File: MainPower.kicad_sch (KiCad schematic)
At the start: 70 parts, among them Q2 MBT2222ADW1T1, Q3 MBT2222ADW1T1, U10 ADM1176-1ARMZ-R7, U5 TPS259621DDA, U6 TPS54226PWPR, U7 ADM1176-1ARMZ-R7, U8 TPS259621DDA, U9 TPS54226PWPR

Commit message: v4.0 Updates
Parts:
- added R41: 100k, Resistor_SMD:R_0603_1608Metric, symbol Device:R_Small
- renumbered C31 to C29, C32 to C30, C33 to C31, C34 to C32, C35 to C33, C36 to C34, C37 to C35, C38 to C36, C39 to C37, C40 to C38, C41 to C39, C53 to C55, D8 to D10, D3 to D5, D4 to D6, D5 to D7, D6 to D8, D7 to D9, Q2 to Q3, Q3 to Q4, R20 to R22, R21 to R23, R22 to R24, R23 to R25, R24 to R26, R25 to R27, R26 to R28, R27 to R29, R29 to R30, R160 to R40, R41 to R42
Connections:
- net 3V3_P_EN: now also R41.1
- net GND: now also R41.2
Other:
- sheet I2C Protection5 renamed I2C Protection
- sheet I2C Protection7 renamed I2C Protection1
- moved on the sheet: R40

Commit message: DFM updates
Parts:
- C29, C42: DPN 587-3473-1-ND -> (none); DST Digi-Key -> (none); MFR Taiyo Yuden -> (none); MPN TMK107BJ105KAHT -> C2803395
- C30, C43: DPN 490-GCM32EC71E226KE36KCT-ND -> (none); DST Digi-Key -> (none); MFR Murata Electronics -> (none); MPN GCM32EC71E226KE36K -> C2214844
- C31, C44: DPN 399-14102-1-ND -> (none); DST Digi-Key -> (none); MFR KEMET -> (none); MPN C0603C103J3GECAUTO -> C161232
- C32, C33, C45, C46, C55: MPN (none) -> C386084
- C34, C39, C47, C52: MPN (none) -> C3877267
- C35, C48: MPN (none) -> C307348
- C36, C49: MPN (none) -> C2214844
- C37, C38, C50, C51: MPN (none) -> C2803395
- D5, D6, D7, D8: Author Antmicro -> (none); License Apache-2.0 -> (none); MPN LTST-C190GKT -> C2909774; Manufacturer Lite-On -> (none); Public False -> (none)
- L2, L3: Flight SPM5030T-3R3M-HZ -> (none); MPN (none) -> C518955; Manufacturer_Name TAI-TECH -> (none); Manufacturer_Part_Number HPC5040NF-3R3MTH -> (none); Proto HPC5040NF-3R3MTH -> (none)
- Q3: Flight MBT2222ADW1T1G -> (none); Manufacturer_Name ON Semiconductor -> (none); Manufacturer_Part_Number MBT2222ADW1T1G -> (none); Proto MBT2222ADW1T1G -> (none)
- R22: DPN RMCF0603FT10K0CT-ND -> (none); DST Digi-Key -> (none); MFR Stackpole Electronics Inc -> (none); MPN RMCF0603FT10K0 -> C844743
- R23: DPN RMCF0603FT10K0CT-ND -> (none); DST Digi-Key -> (none); MFR Stackpole Electronics Inc -> (none); MPN RMCF0603FT10K0 -> C844363
- R24: DPN RMCF0603FT604RCT-ND -> (none); DST Digi-Key -> (none); MFR Stackpole Electronics Inc -> (none); MPN RMCF0603FT604R -> C2091072
- R25, R35, R48: MPN (none) -> C843966
- R26, R36: MPN (none) -> C844759
- R27, R37, R49, R51: MPN (none) -> C237792
- R28, R38: value 0.01R -> 10m; MPN (none) -> C840621
- R29, R39: MPN (none) -> C2484712
- R30, R31, R43: MPN (none) -> C844915
- R32: DPN RMCF0603FT10K0CT-ND -> (none); DST Digi-Key -> (none); MFR Stackpole Electronics Inc -> (none); MPN RMCF0603FT10K0 -> C844796
- R33: DPN RMCF0603FT10K0CT-ND -> (none); DST Digi-Key -> (none); MFR Stackpole Electronics Inc -> (none); MPN RMCF0603FT10K0 -> C844734
- R40: DPN RMCF0603FT604RCT-ND -> (none); DST Digi-Key -> (none); MFR Stackpole Electronics Inc -> (none); MPN RMCF0603FT604R -> C2479067
- R41: DPN RMCF0603FT604RCT-ND -> (none); DST Digi-Key -> (none); MFR Stackpole Electronics Inc -> (none); MPN RMCF0603FT604R -> C237792
- R42: MPN (none) -> C402995
- R44, R45: Author Antmicro -> (none); License Apache-2.0 -> (none); MPN CR0402-FX-4701GLF -> C2479067; Manufacturer Bourns -> (none); Tolerance 1% -> (none); Val 4k7 -> (none)
- R46, R47: Author Antmicro -> (none); License Apache-2.0 -> (none); MPN CR0402-FX-4701GLF -> C844931; Manufacturer Bourns -> (none); Tolerance 1% -> (none); Val 4k7 -> (none)
- R50: MPN (none) -> C118142
- R52: MPN (none) -> C844923
- R53: MPN (none) -> C2479067
- U5, U8: DPN 296-TPS259620DDATCT-ND -> (none); DST Digi-Key -> (none); MFR Texas Instruments -> (none); MPN TPS259620DDAT -> C2155774

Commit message: Minor schematic fixes
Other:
- note added: "Vout = 0.765 * (1 + R25 / R26) Vout = 0.765 * (1 + 73.2k / 22.1k) Vout - 3.298V"
- note added: "Vout = 0.765 * (1 + R35 / R36) Vout = 0.765 * (1 + 73.2k / 22.1k) Vout - 3.298V"
- note removed: "Vout = 0.765 * (1 + R114 / R115) Vout = 0.765 * (1 + 73.2k / 22.1k) Vout - 3.298V"
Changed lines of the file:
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@@
 		)
 	)
-	(text "Vout = 0.765 * (1 + R114 / R115)\nVout = 0.765 * (1 + 73.2k / 22.1k)\nVout - 3.298V"
+	(text "Vout = 0.765 * (1 + R35 / R36)\nVout = 0.765 * (1 + 73.2k / 22.1k)\nVout - 3.298V"
 		(exclude_from_sim no)
 		(at 116.84 136.906 0)
@@
 		)
 	)
-	(text "Vout = 0.765 * (1 + R114 / R115)\nVout = 0.765 * (1 + 73.2k / 22.1k)\nVout - 3.298V"
+	(text "Vout = 0.765 * (1 + R25 / R26)\nVout = 0.765 * (1 + 73.2k / 22.1k)\nVout - 3.298V"
 		(exclude_from_sim no)
 		(at 112.268 68.326 0)

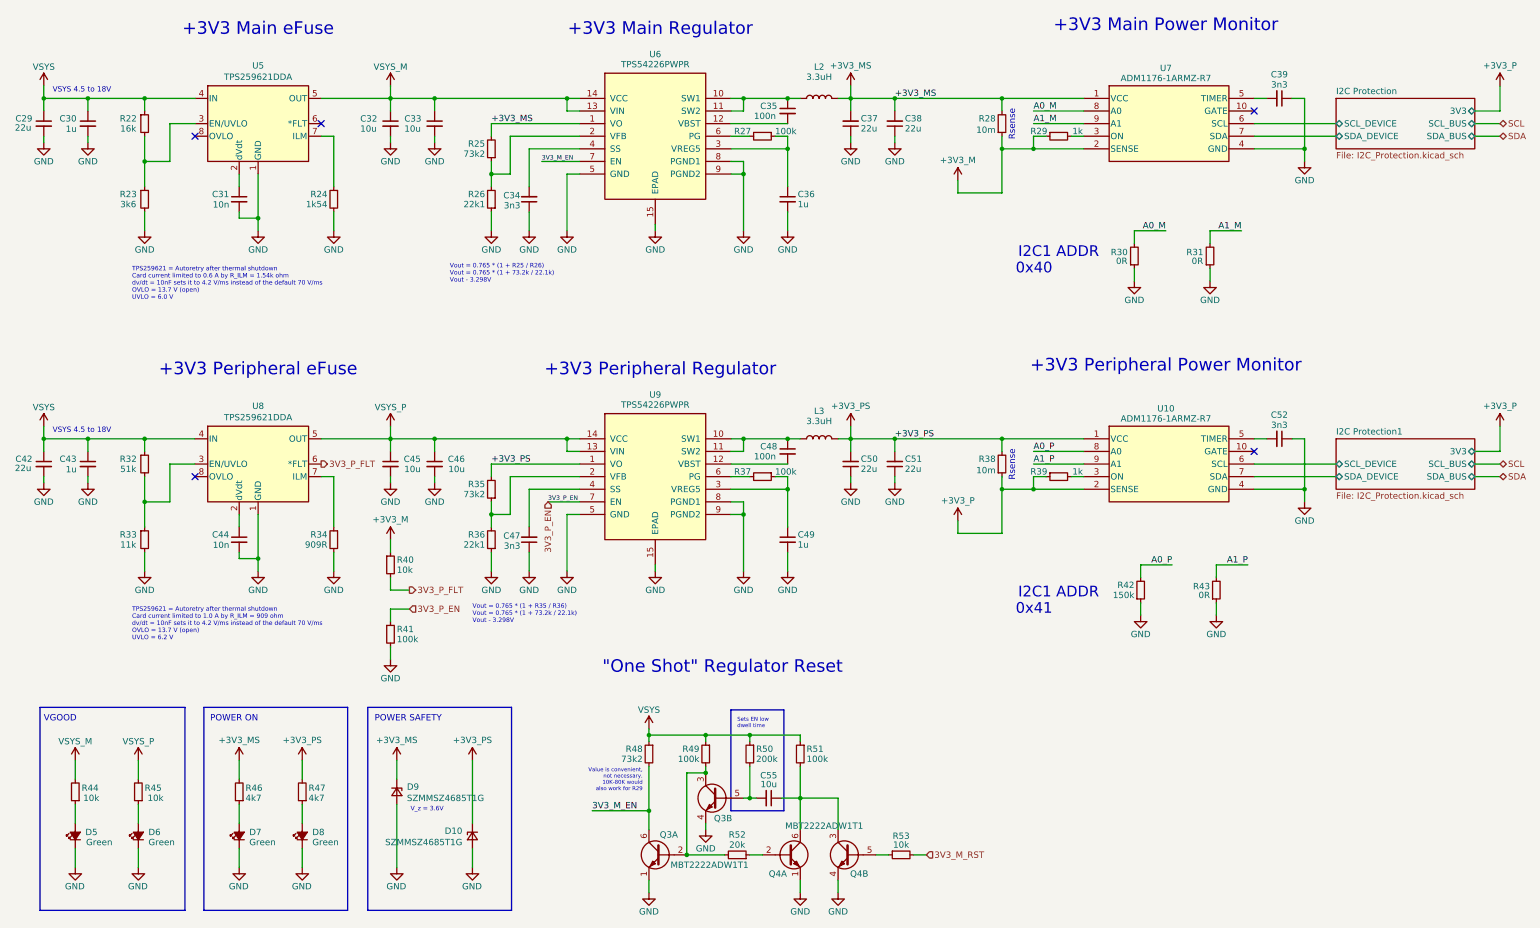
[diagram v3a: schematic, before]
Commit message: Fixed Jetson FPC pinout
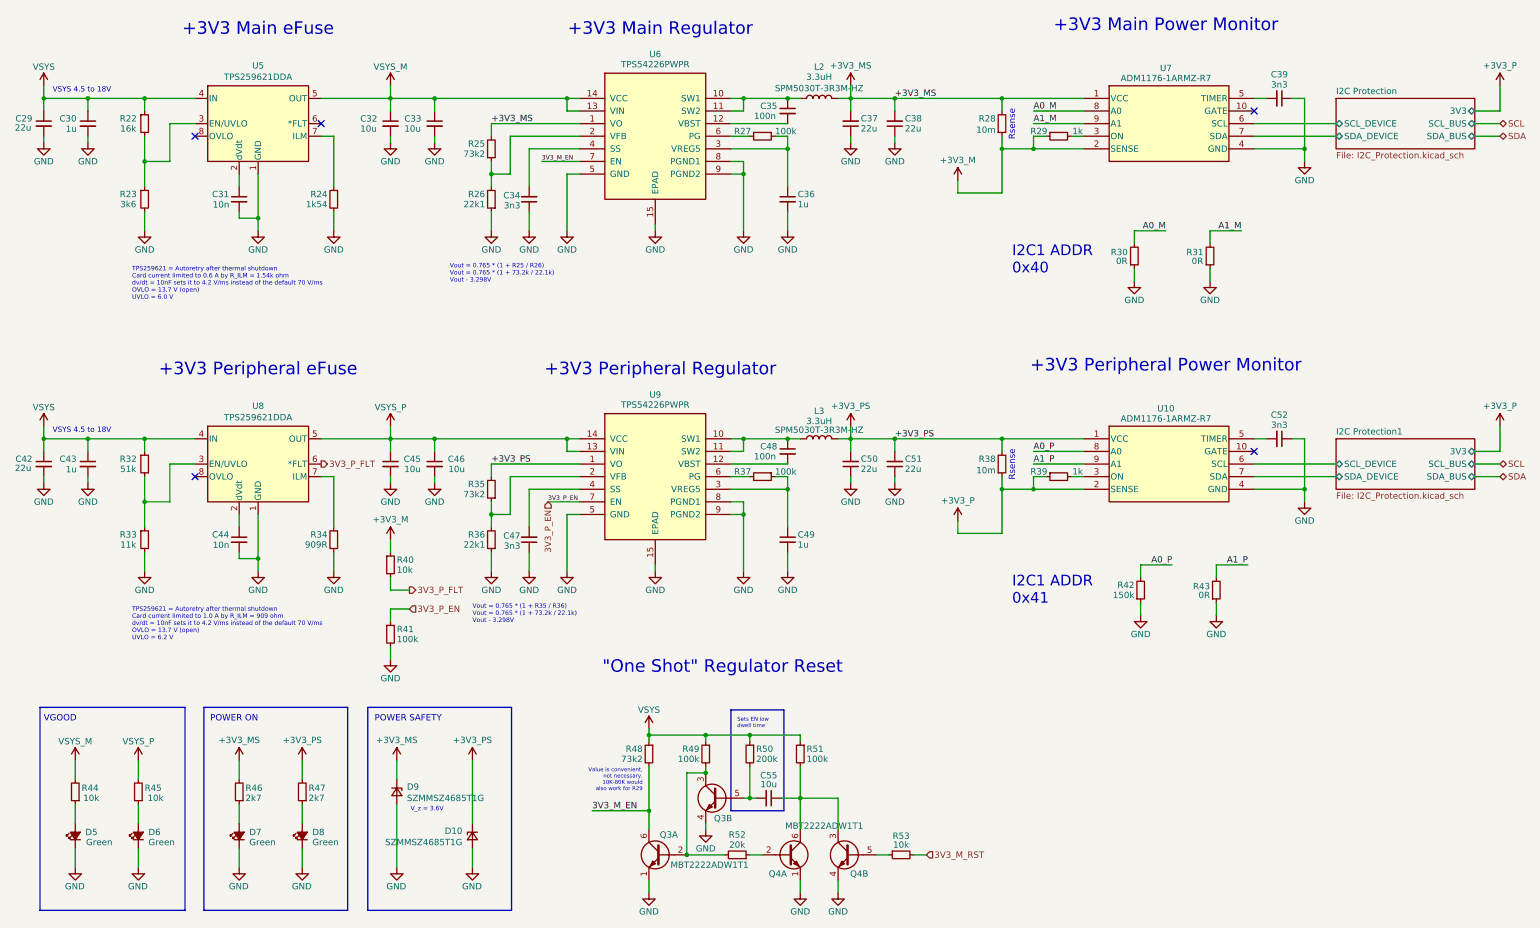
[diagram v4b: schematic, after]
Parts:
- L2, L3: Field6 (none) -> SPM5030T-3R3M-HZ
- R46, R47: value 4k7 -> 2k7; MPN C844931 -> C237112
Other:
- note added: "I2C1 ADDR 0x40"
- note added: "I2C1 ADDR 0x41"
- note removed: "0x40"
- note removed: "0x41"
- note removed: "I2C1 ADDR"
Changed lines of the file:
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@@
 		)
 	)
-	(text "I2C1 ADDR"
+	(text "I2C1 ADDR\n0x41"
 		(exclude_from_sim no)
-		(at 243.078 133.858 0)
+		(at 225.552 135.128 0)
 		(effects
 			(font
 				(size 2.159 2.159)
 			)
-			(justify right bottom)
+			(justify left bottom)
 		)
 	)
@@
 		)
 	)
-	(text "0x41"
-		(exclude_from_sim no)
-		(at 233.68 137.16 0)
-		(effects
-			(font
-				(size 2.159 2.159)
-			)
-			(justify right bottom)
-		)
-	)
 	(text "Value is convenient,\nnot necessary. \n10K-80K would\nalso work for R29"
 		(exclude_from_sim no)
@@
 		)
 	)
-	(text "0x40"
-		(exclude_from_sim no)
-		(at 233.68 68.58 0)
-		(effects
-			(font
-				(size 2.159 2.159)
-			)
-			(justify right bottom)
-		)
-	)
 	(text "TPS259621 = Autoretry after thermal shutdown\nCard current limited to 1.0 A by R_ILM = 909 ohm\ndv/dt = 10nF sets it to 4.2 V/ms instead of the default 70 V/ms\nOVLO = 13.7 V (open)\nUVLO = 6.2 V"
 		(exclude_from_sim no)
@@
 		)
 	)
-	(text "I2C1 ADDR"
+	(text "I2C1 ADDR\n0x40"
 		(exclude_from_sim no)
-		(at 243.078 65.278 0)
+		(at 225.552 68.58 0)
 		(effects
 			(font
 				(size 2.159 2.159)
 			)
-			(justify right bottom)
+			(justify left bottom)
 		)
 	)
@@
 			)
 		)
-		(property "Value" "4k7"
+		(property "Value" "2k7"
 			(at 83.82 173.228 0)
 			(effects
@@
 			)
 		)
-		(property "MPN" "C844931"
+		(property "MPN" "C237112"
 			(at 82.55 172.72 0)
 			(effects
@@
 			)
 		)
-		(property "Value" "4k7"
+		(property "Value" "2k7"
 			(at 71.12 173.228 0)
 			(effects
@@
 			)
 		)
-		(property "MPN" "C844931"
+		(property "MPN" "C237112"
 			(at 69.85 172.72 0)
 			(effects
@@
 			)
 		)
+		(property "Field6" "SPM5030T-3R3M-HZ"
+			(at 186.69 30.988 90)
+			(effects
+				(font
+					(size 1.27 1.27)
+				)
+			)
+		)
 		(pin "1"
 		)
@@
 			)
 		)
+		(property "Field6" "SPM5030T-3R3M-HZ"
+			(at 186.69 99.822 90)
+			(effects
+				(font
+					(size 1.27 1.27)
+				)
+			)
+		)

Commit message: v4.2 Updates
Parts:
- added D16, D3: DFLS130LQ-7, Diode_SMD:D_PowerDI-123, symbol Device:D_Schottky_Small
- U6, U9: footprint Package_SO:HTSSOP-14-1EP_4.4x5mm_P0.65mm_EP3.4x5mm_Mask3x3.1mm -> Package_SO:TSSOP-14-1EP_4.4x5mm_P0.65mm
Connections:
- net VSYS_M: now also D3.1 (K)
- net VSYS_P: now also D16.1 (K)
- new net VUSB: D16.2 (A), D3.2 (A)
